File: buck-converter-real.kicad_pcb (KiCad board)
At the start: 4 copper layers, 64 x 32 mm, 45 parts, among them J1 Conn_01x02_Pin, J2 XT60, J3 Battery out (3V6-4V2) NiMH 3S, J6 DM3CS-SF, Q2 CSD18540Q5B - 60-V, U1 AP2112K-3.3 (3V3 LDO), U5 LM5109BMA (Mosfet Driver), U6 AS78L12RTR-G1 (12V LDO)

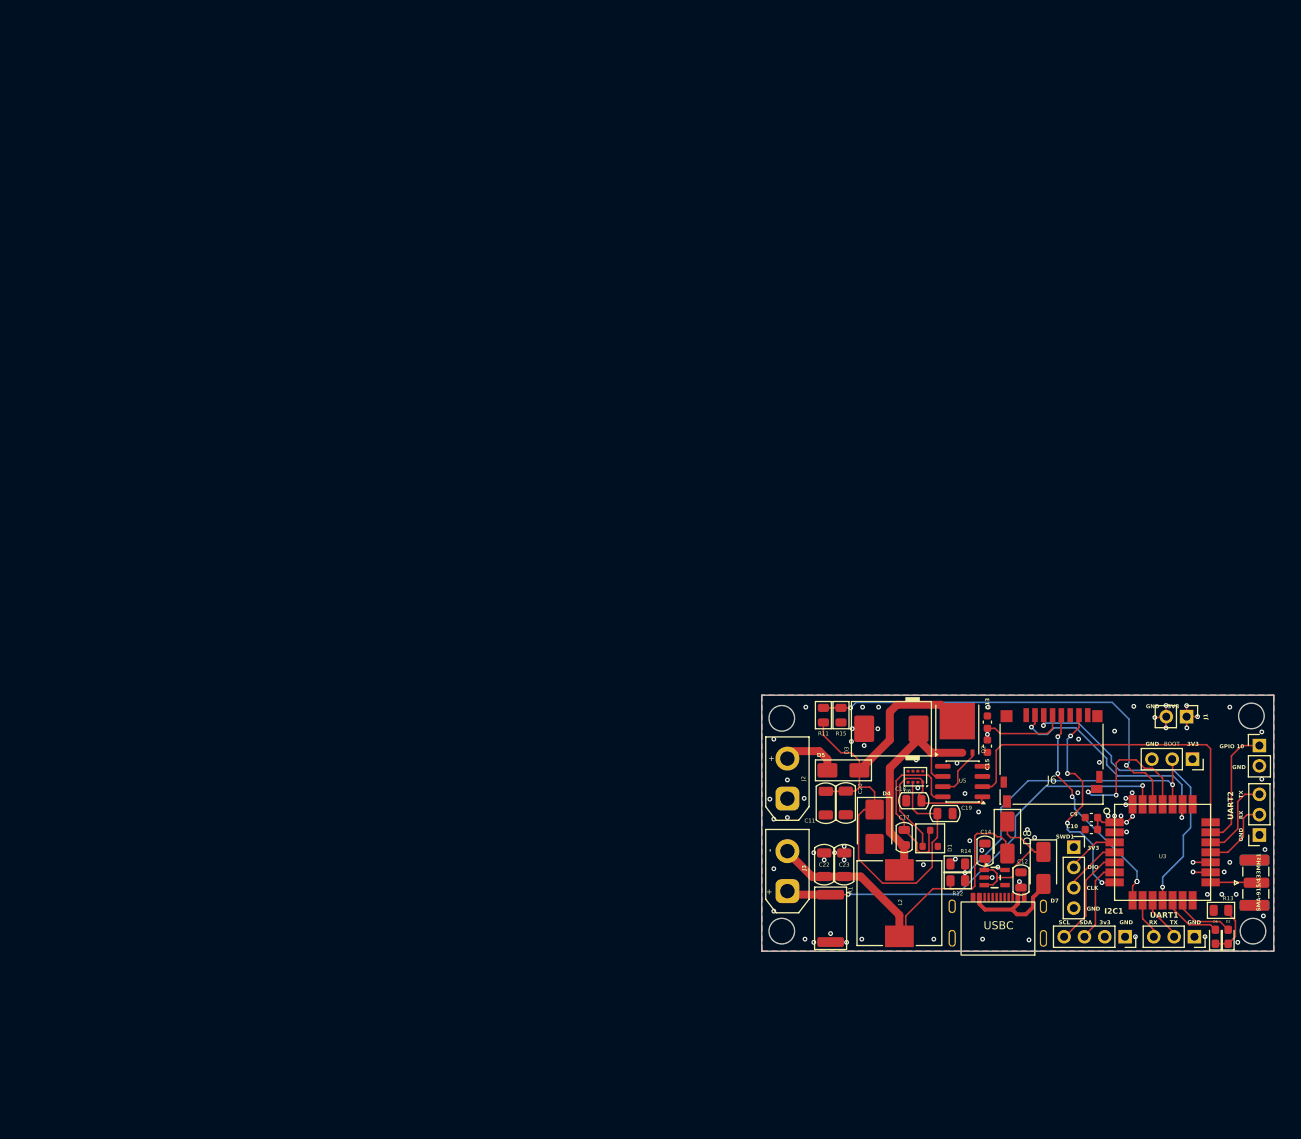
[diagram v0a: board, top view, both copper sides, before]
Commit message: Update layout - after successful board test
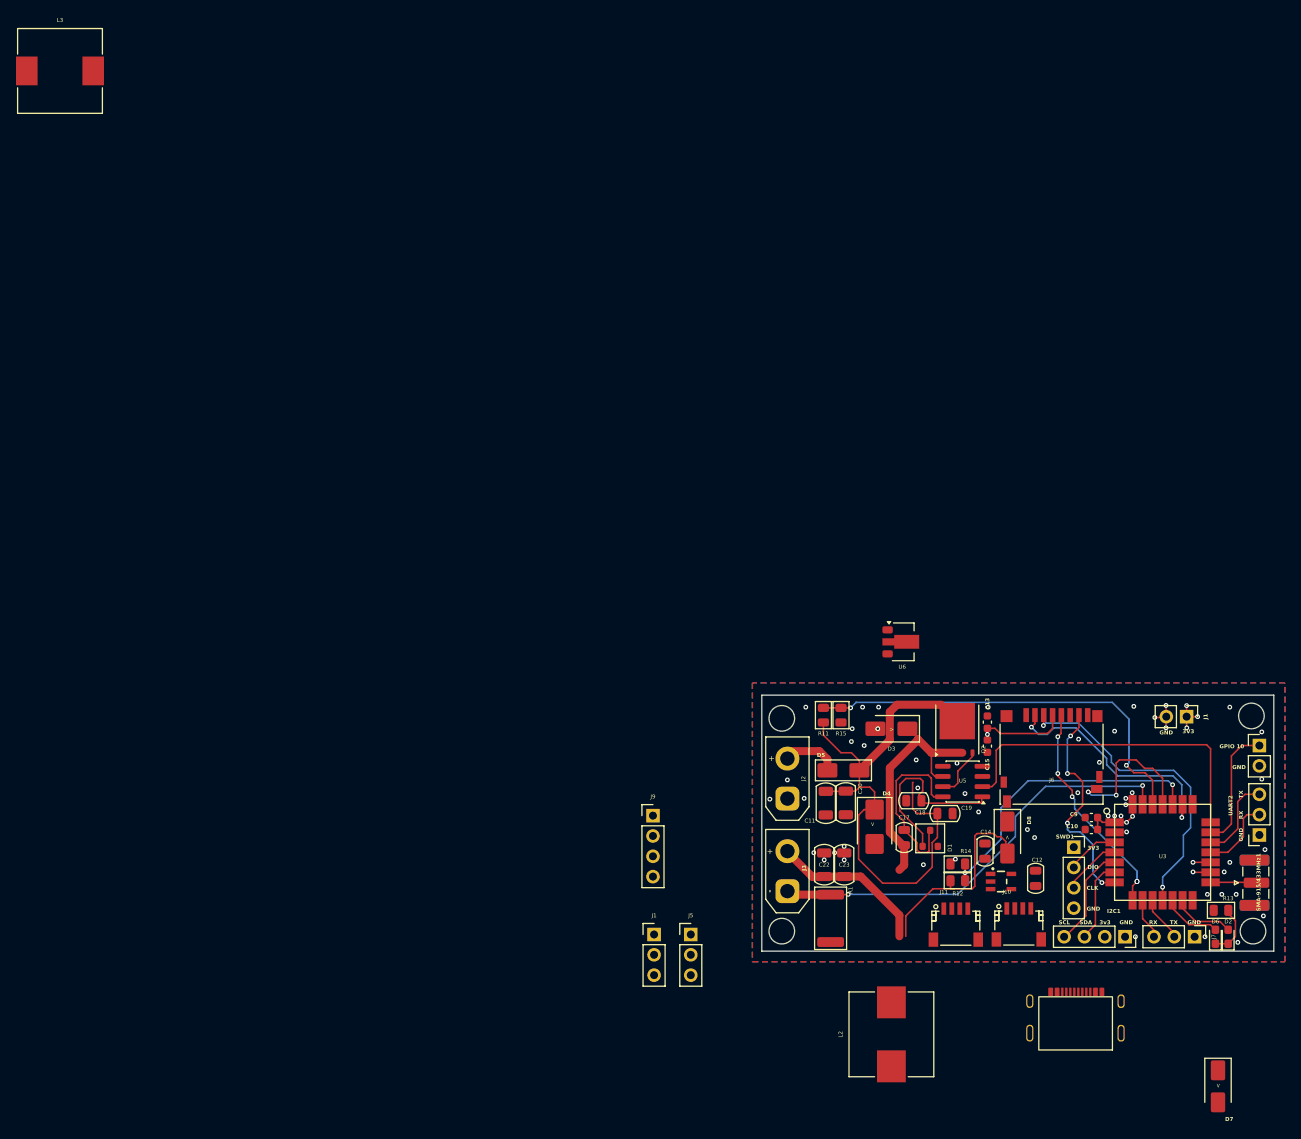
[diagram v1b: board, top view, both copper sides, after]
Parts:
- removed BOOT1: Boot, Connector_PinSocket_2.54mm:PinSocket_1x03_P2.54mm_Vertical
- removed UART1: UART, Connector_PinSocket_2.54mm:PinSocket_1x03_P2.54mm_Vertical
- added J1: BOOT, Connector_PinHeader_2.54mm:PinHeader_1x03_P2.54mm_Vertical, F.Cu at (80.0, 113.4)
- added J10: JST_01x04, Connectors_JST:JST_SH_SM04B-SRSS-TB_04x1.00mm_Angled, F.Cu at (125.6, 112.1)
- added J11: JST_01x04, Connectors_JST:JST_SH_SM04B-SRSS-TB_04x1.00mm_Angled, F.Cu at (117.8, 112.1)
- added J5: UART 2, Connector_PinHeader_2.54mm:PinHeader_1x03_P2.54mm_Vertical, F.Cu at (84.6, 113.4)
- added J7: UART 1, Connector_PinHeader_2.54mm:PinHeader_1x03_P2.54mm_Vertical, F.Cu at (147.6, 113.7)
- added J9: SWD, Connector_PinHeader_2.54mm:PinHeader_1x04_P2.54mm_Vertical, F.Cu at (79.9, 98.6)
- added L3: 10uH ±20% 18mΩ Molded, Inductor_SMD:L_10.4x10.4_H4.8, F.Cu at (5.78, 5.47)
- D3: footprint PCM_Diode_SMD_AKL:D_SMC -> Diode_SMD:D_SMA
- GPIO1: value Conn_01x02_Pin -> GPIO
- L2: footprint Inductor_SMD:L_10.4x10.4_H4.8 -> buck-forest:L_10.4x10.4_H4.8
- U6: footprint OptoDevice:Broadcom_APDS-9160-003 -> Package_TO_SOT_SMD:SOT-89-3
- moved D7 35.0 mm to (150.5, 132.4)
- moved U6 16.9 mm to (111.2, 76.8), turned to 0 degrees
- moved L2 16.4 mm to (109.7, 125.9)
- moved USBC1 15.3 mm to (132.9, 114.3)
- moved C12 1.84 mm to (127.7, 106.4)
- moved U1 0.94 mm to (123.4, 106.8)
- renumbered U2 to USBC1
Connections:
- net /BOOT renamed /VSENSE_VOUT
- C10 pad 1: GND -> +3.3V
- C10 pad 2: +3.3V -> GND
- C9 pad 1: GND -> +3.3V
- C9 pad 2: +3.3V -> GND
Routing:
- net Net-(D7-K): track 18.9 -> 0.00 mm
- net Net-(D7-A): track 13.7 -> 0.00 mm
- net /VSENSE_VOUT: track 41.6 -> 38.4 mm
- net +3.3V: track 31.1 -> 29.2 mm, vias 14 -> 12
- net GND: track 8.19 -> 7.39 mm, vias 64 -> 48
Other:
- board text added: ">"
- board text removed: "BOOT"
- board text removed: "USBC"

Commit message: Update schematic - adding ch32
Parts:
- added U2: CH32V203K8T6, forest-ch:LQFP-32_L7.0-W7.0-P0.80-LS9.0-BL, F.Cu at (110.5, 150.6)
- added Y1: 8MHz 20pF HC-49S-SMD, forest-ch:CRYSTAL-SMD_L11.4-W4.8-LS12.7, F.Cu at (126.9, 154.0)
- J1: value BOOT -> USB_C_Receptacle_USB2.0_16P; footprint Connector_PinHeader_2.54mm:PinHeader_1x03_P2.54mm_Vertical -> Connector_USB:USB_C_Receptacle_G-Switch_GT-USB-7010ASV
- U6: value AS78L12RTR-G1 (12V LDO) -> 78L12L (12V LDO) (35V max)

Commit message: Update layout - enlarge board
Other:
- board size 64 x 32 mm -> 64 x 64 mm
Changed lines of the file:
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@@
 	(gr_rect
 		(start 93.5 83.5)
-		(end 157.5 115.5)
+		(end 157.5 147.5)
 		(radius 2)
 		(stroke
@@
 	(zone
 		(net "+3.3V")
+		(locked yes)
 		(layer "In2.Cu")
 		(hatch edge 0.5)
@@
 		(polygon
 			(pts
-				(xy 154.906426 86.007976) (xy 95.997383 86.371628) (xy 96.003219 113.18141) (xy 154.893587 113.168591)
+				(xy 154.906426 86.007976) (xy 95.997383 86.371628) (xy 96.010174 145.131409) (xy 154.878484 145.118594)
 			)
 		)

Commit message: Update layout - Swap to square board
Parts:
- removed D7, D8: SS34 - 40V 3A, Diode_SMD:D_SMA
- removed I2C1: I2C1, Connector_PinSocket_2.54mm:PinSocket_1x04_P2.54mm_Vertical
- removed SWD1: SWD, Connector_PinSocket_2.54mm:PinSocket_1x04_P2.54mm_Vertical
- removed UART2: UART, Connector_PinSocket_2.54mm:PinSocket_1x03_P2.54mm_Vertical
- removed USBC1: ~, buck-mppt:USB-CD16HMXTR
- added C26: 15pF C0G 50V, Capacitor_SMD:C_0805_2012Metric_Pad1.18x1.45mm_HandSolder, F.Cu at (229.7, 135.5)
- added C33: 15pF C0G 50V, Capacitor_SMD:C_0805_2012Metric_Pad1.18x1.45mm_HandSolder, F.Cu at (229.5, 132.6)
- added D10: LED, LED_SMD:LED_0603_1608Metric_Pad1.05x0.95mm_HandSolder, F.Cu at (237.0, 130.3)
- added D11: LED, LED_SMD:LED_0603_1608Metric_Pad1.05x0.95mm_HandSolder, F.Cu at (237.0, 132.9)
- added D12: SS34 40V 3A, Diode_SMD:D_SMA, F.Cu at (177.5, 119.9)
- added D13: SS34 40V 3A, Diode_SMD:D_SMA, F.Cu at (215.0, 51.9)
- J9: footprint Connector_PinHeader_2.54mm:PinHeader_1x04_P2.54mm_Vertical -> Connector_JST:JST_XH_B4B-XH-AM_1x04_P2.50mm_Vertical
- Y1: value 8MHz 20pF HC-49S-SMD -> 8MHz 20pF
- moved L3 185.2 mm to (179.1, 70.8)
- moved J1 140.4 mm to (218.8, 135.1)
- moved U2 117.9 mm to (223.7, 117.5)
- moved GPIO1 101.2 mm to (256.5, 80.8)
- moved C11 101.2 mm to (202.3, 88.0)
- moved C12 101.2 mm to (228.5, 97.4)
- moved C14 101.2 mm to (222.2, 94.0)
- moved C18 101.2 mm to (213.3, 87.7)
- moved C19 101.2 mm to (217.2, 89.3)
- moved C20 101.2 mm to (204.8, 88.0)
- moved D4 101.2 mm to (208.4, 90.9)
- moved J1 101.2 mm to (247.4, 77.2)
- moved J10 101.2 mm to (226.4, 103.1)
- moved J11 101.2 mm to (218.5, 103.1)
- moved J5 101.2 mm to (185.4, 104.4)
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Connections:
- J1 pad A1: Net-(J1-GND-PadA1) -> GND
- J1 pad A12: Net-(J1-GND-PadA1) -> GND
- J1 pad A5: unconnected-(J1-CC1-PadA5) -> Net-(J1-CC1)
- J1 pad A6: unconnected-(J1-D+-PadA6) -> Net-(U2-PA12/USB1DP)
- J1 pad A7: unconnected-(J1-D--PadA7) -> Net-(U2-PA11/USB1DM)
- J1 pad B1: Net-(J1-GND-PadA1) -> GND
- J1 pad B12: Net-(J1-GND-PadA1) -> GND
- J1 pad B5: unconnected-(J1-CC2-PadB5) -> Net-(J1-CC2)
- J1 pad B6: unconnected-(J1-D+-PadB6) -> Net-(U2-PA12/USB1DP)
- J1 pad B7: unconnected-(J1-D--PadB7) -> Net-(U2-PA11/USB1DM)
- J1 pad SH: unconnected-(J1-SHIELD-PadSH) -> GND
- J9 pad 2: /SWDIO -> /SWD-WIO-IO
- J9 pad 3: /SWCLK -> /SWD-WIO-CLK
- U2 pad 1: unconnected-(U2-VDD-Pad1) -> +3.3V
- U2 pad 16: unconnected-(U2-VSS-Pad16) -> GND
- U2 pad 17: unconnected-(U2-VDD-Pad17) -> +3.3V
- U2 pad 19: unconnected-(U2-PA9-Pad19) -> /UART-WIO-TX
- U2 pad 2: unconnected-(U2-OSC_IN/PD0-Pad2) -> Net-(U2-OSC_IN/PD0)
- U2 pad 20: unconnected-(U2-PA10-Pad20) -> /UART-WIO-RX
- U2 pad 21: unconnected-(U2-PA11/USB1DM-Pad21) -> Net-(U2-PA11/USB1DM)
- U2 pad 22: unconnected-(U2-PA12/USB1DP-Pad22) -> Net-(U2-PA12/USB1DP)
- U2 pad 23: unconnected-(U2-PA13/SWDIO-Pad23) -> /CH-SWD-IO
- U2 pad 24: unconnected-(U2-PA14/SWCLK-Pad24) -> /CH-SWD-CLK
- U2 pad 29: unconnected-(U2-PB6-Pad29) -> /SWD-WIO-IO
- U2 pad 3: unconnected-(U2-OSC_OUT/PD1-Pad3) -> Net-(U2-OSC_OUT/PD1)
- U2 pad 30: unconnected-(U2-PB7-Pad30) -> /SWD-WIO-CLK
- U2 pad 31: unconnected-(U2-PB8/BOOT0-Pad31) -> Net-(U2-PB8/BOOT0)
- U2 pad 32: unconnected-(U2-VSS-Pad32) -> GND
- U2 pad 4: unconnected-(U2-NRST-Pad4) -> Net-(U2-NRST)
- U2 pad 5: unconnected-(U2-VDDA-Pad5) -> +3.3V
- Y1 pad 1: unconnected-(Y1-Pad1) -> Net-(U2-OSC_IN/PD0)
- Y1 pad 2: unconnected-(Y1-Pad2) -> Net-(U2-OSC_OUT/PD1)
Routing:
- net Net-(D4-K): track 70.7 -> 0.00 mm
- net /BAT_ISENSE: track 54.2 -> 0.00 mm, vias 2 -> 0
- net /VSENSE_VIN: track 52.3 -> 0.00 mm, vias 2 -> 0
- net +BATT: track 48.3 -> 0.00 mm
- net /PWM_HI: track 42.4 -> 0.00 mm
- net /SPI-COTI: track 39.2 -> 0.00 mm, vias 2 -> 0
- net /VSENSE_VOUT: track 38.4 -> 0.00 mm, vias 2 -> 0
- net /SPI-CS: track 30.4 -> 0.00 mm, vias 2 -> 0
- net Net-(D3-K): track 29.8 -> 0.00 mm
- net +3.3V: track 29.2 -> 0.00 mm, vias 12 -> 0
- net /SPI-CITO: track 27.9 -> 0.00 mm, vias 4 -> 0
- net /SPI-SCK: track 27.7 -> 0.00 mm, vias 5 -> 0
- net Net-(D1-A2): track 23.7 -> 0.00 mm
- net Net-(D1-K): track 22.5 -> 0.00 mm
- net /GPIO-9: track 19.3 -> 0.00 mm, vias 2 -> 0
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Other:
- outline, holes or cut-outs redrawn
- board text removed: "3v3"
- board text removed: "CLK"
- board text removed: "DIO"
- board text removed: "SDA"

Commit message: Update layout - Inital layout for new form factor
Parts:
- added R25: 5.1K, Resistor_SMD:R_0805_2012Metric_Pad1.20x1.40mm_HandSolder, F.Cu at (127.9, 118.5)
- added R26: 5.1K, Resistor_SMD:R_0805_2012Metric_Pad1.20x1.40mm_HandSolder, F.Cu at (127.9, 121.4)
- added RST1: SW_Omron_B3FS, Button_Switch_SMD:SW_SPST_Omron_B3FS-100xP, F.Cu at (99.8, 74.0)
- added SW2: SW_Omron_B3FS, Button_Switch_SMD:SW_SPST_Omron_B3FS-100xP, F.Cu at (141.8, 123.2)
- J10: value JST_01x04 -> I2C1; footprint Connectors_JST:JST_SH_SM04B-SRSS-TB_04x1.00mm_Angled -> Connector_JST:JST_SH_BM04B-SRSS-TB_1x04-1MP_P1.00mm_Vertical
- J11: footprint Connectors_JST:JST_SH_SM04B-SRSS-TB_04x1.00mm_Angled -> Connector_JST:JST_SH_BM04B-SRSS-TB_1x04-1MP_P1.00mm_Vertical
- J2: value XT60 -> SOL 24V
- J9: footprint Connector_JST:JST_XH_B4B-XH-AM_1x04_P2.50mm_Vertical -> Connector_JST:JST_PH_B4B-PH-K_1x04_P2.00mm_Vertical
- moved J10 183.4 mm to (43.0, 100.5)
- moved J11 175.6 mm to (43.0, 108.8)
- moved L3 163.9 mm to (22.4, 22.7)
- moved J6 147.1 mm to (83.4, 78.5)
- moved GPIO1 146.4 mm to (115.9, 40.1)
- moved J1 146.4 mm to (106.8, 36.5)
- moved J9 140.9 mm to (39.8, 91.2)
- moved J5 140.0 mm to (50.2, 68.0)
- moved D13 132.2 mm to (101.8, 120.0)
- moved U6 130.0 mm to (85.0, 95.8)
- moved C11 127.6 mm to (75.3, 100.5)
- moved C18 127.6 mm to (86.3, 100.2)
- moved C19 127.6 mm to (90.2, 101.8)
- moved C20 127.6 mm to (77.8, 100.5)
- moved Q2 127.6 mm to (91.7, 91.3)
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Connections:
- net /I2C-SCL renamed /I2C-1-SCL
- net /I2C-SDA renamed /I2C-1-SDA
- D2 pad 2: /LED1 -> /LED2
- D6 pad 2: /LED2 -> /LED1
- J11 pad 1: unconnected-(J11-Pin_1-Pad1) -> /I2C-2-SCL
- J11 pad 2: unconnected-(J11-Pin_2-Pad2) -> /I2C-2-SCA
- J6 pad 9: /GPIO-9 -> unconnected-(J6-CDS-Pad9)
- U3 pad 12: /LED2 -> /I2C-2-SCA
- U3 pad 13: /LED1 -> /I2C-2-SCL
- U3 pad 20: /GPIO-10 -> /LED2
- U3 pad 25: /GPIO-9 -> /LED1
- U3 pad 3: /SWDIO -> /SWD-WIO-IO
- U3 pad 4: /SWCLK -> /SWD-WIO-CLK
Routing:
- net Net-(SMA-915/433MHz1-In): track 0.00 -> 6.15 mm
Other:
- board text removed: "3V3"
- board text removed: ">"
- board text removed: "GPIO 10"
- board text removed: "RX"
- board text removed: "SCL"
- board text removed: "TX"

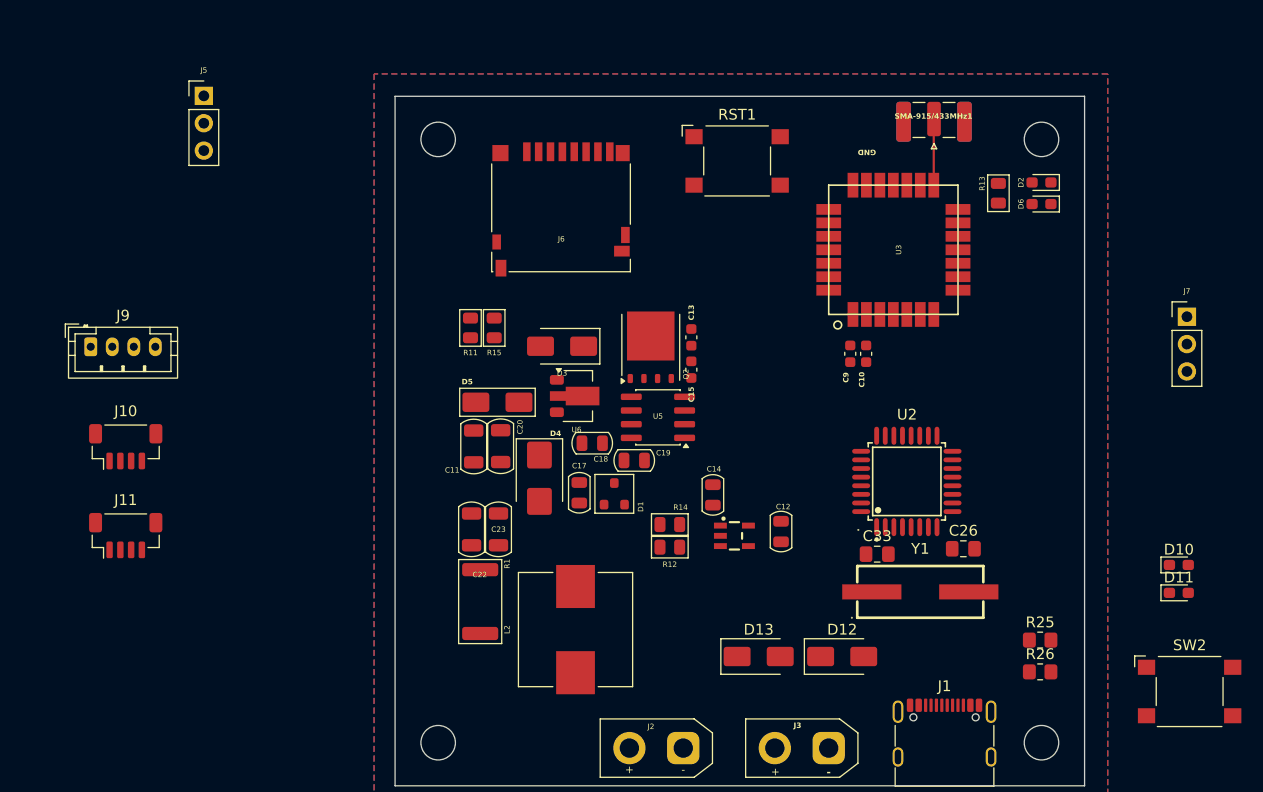
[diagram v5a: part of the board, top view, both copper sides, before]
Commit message: Update layout/schematic - add uart to ch chip
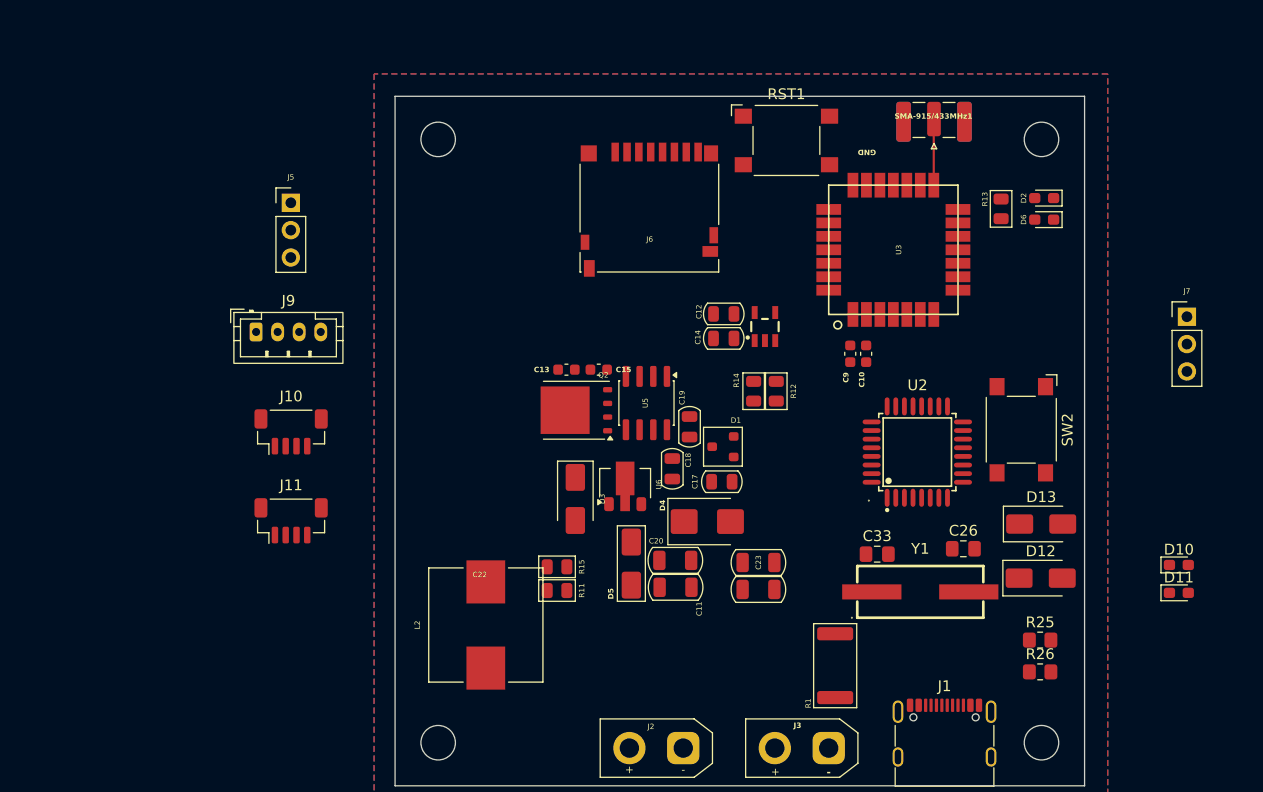
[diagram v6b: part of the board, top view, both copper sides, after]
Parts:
- moved R1 33.5 mm to (108.8, 120.8), turned to -90 degrees
- moved D13 29.0 mm to (128.0, 107.7)
- moved SW2 28.9 mm to (126.1, 99.0), turned to -90 degrees
- moved C22 27.2 mm to (101.7, 113.8), turned to 180 degrees
- moved R11 25.7 mm to (83.0, 113.9), turned to 180 degrees
- moved C23 24.3 mm to (101.7, 111.3), turned to 180 degrees
- moved R15 22.9 mm to (83.0, 111.7), turned to 0 degrees
- moved C11 22.8 mm to (94.0, 113.6), turned to 0 degrees
- moved C12 20.9 mm to (98.5, 88.2), turned to 180 degrees
- moved D12 19.8 mm to (127.9, 112.7)
- moved U1 19.6 mm to (102.3, 89.4), turned to 90 degrees
- moved D5 19.5 mm to (89.9, 111.4), turned to -90 degrees
- moved C20 19.4 mm to (94.0, 111.1), turned to 0 degrees
- moved R12 17.5 mm to (103.4, 95.4), turned to 90 degrees
- moved D4 16.1 mm to (97.0, 107.5), turned to 0 degrees
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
